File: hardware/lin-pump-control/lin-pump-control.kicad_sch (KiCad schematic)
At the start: 27 parts, among them J1 UPDI, J2 I2C LCD, J3 LINBus, Q1 2N7002, Q2 2N7002, U1 TJA1021T, U2 ATtiny824-X, U3 PCA9536DP

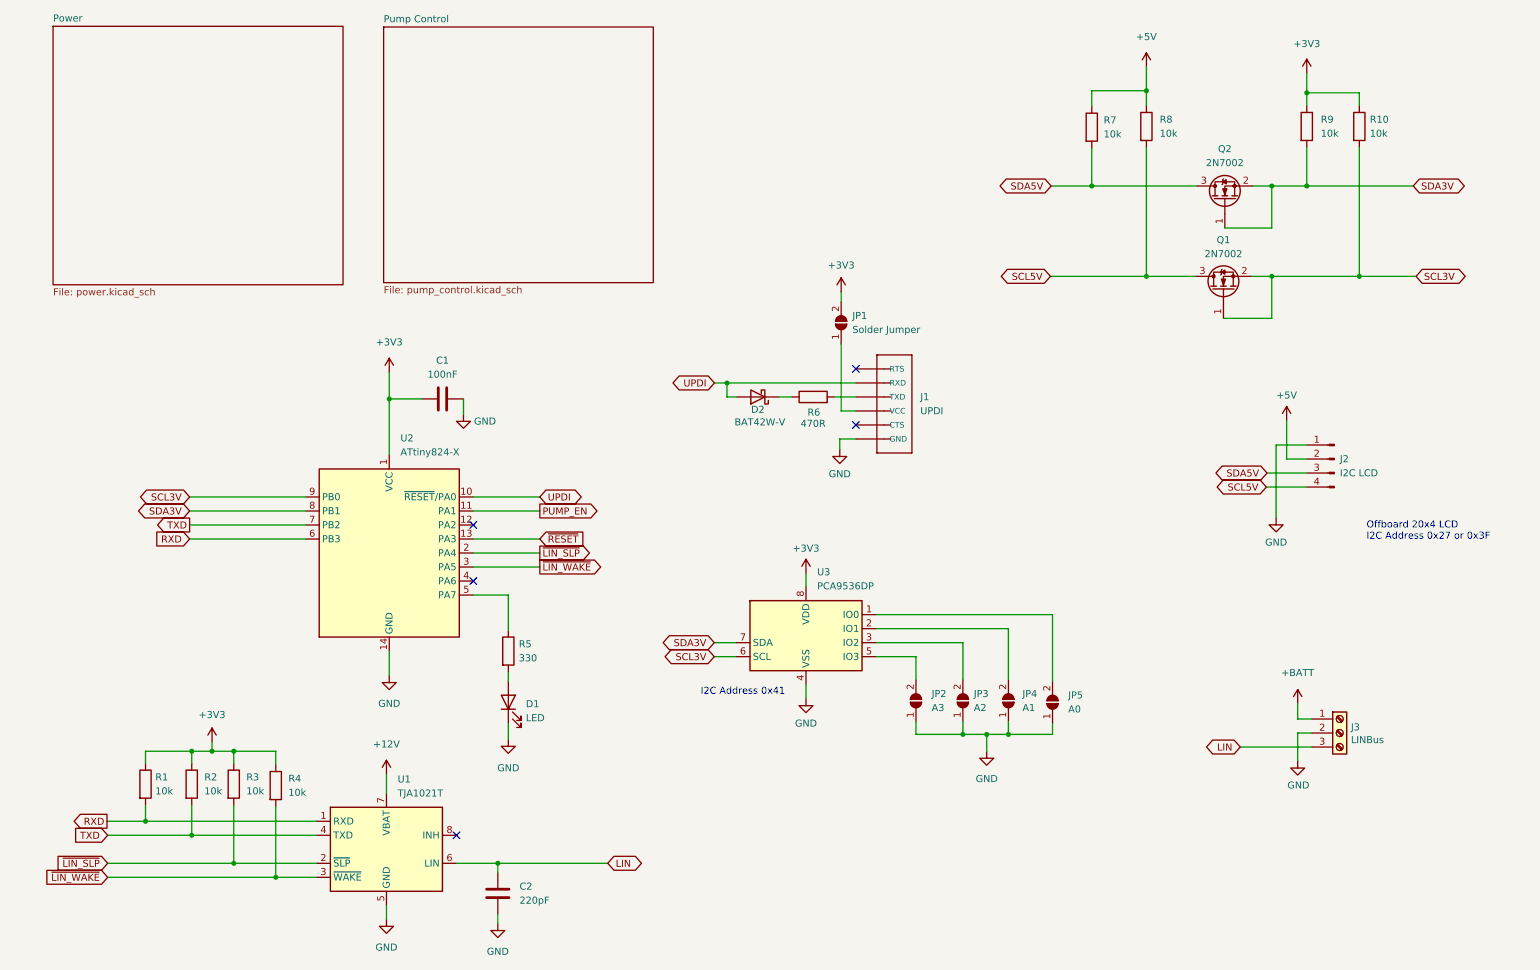
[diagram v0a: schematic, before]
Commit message: Add INA219 to pump controller, change to using regulator module
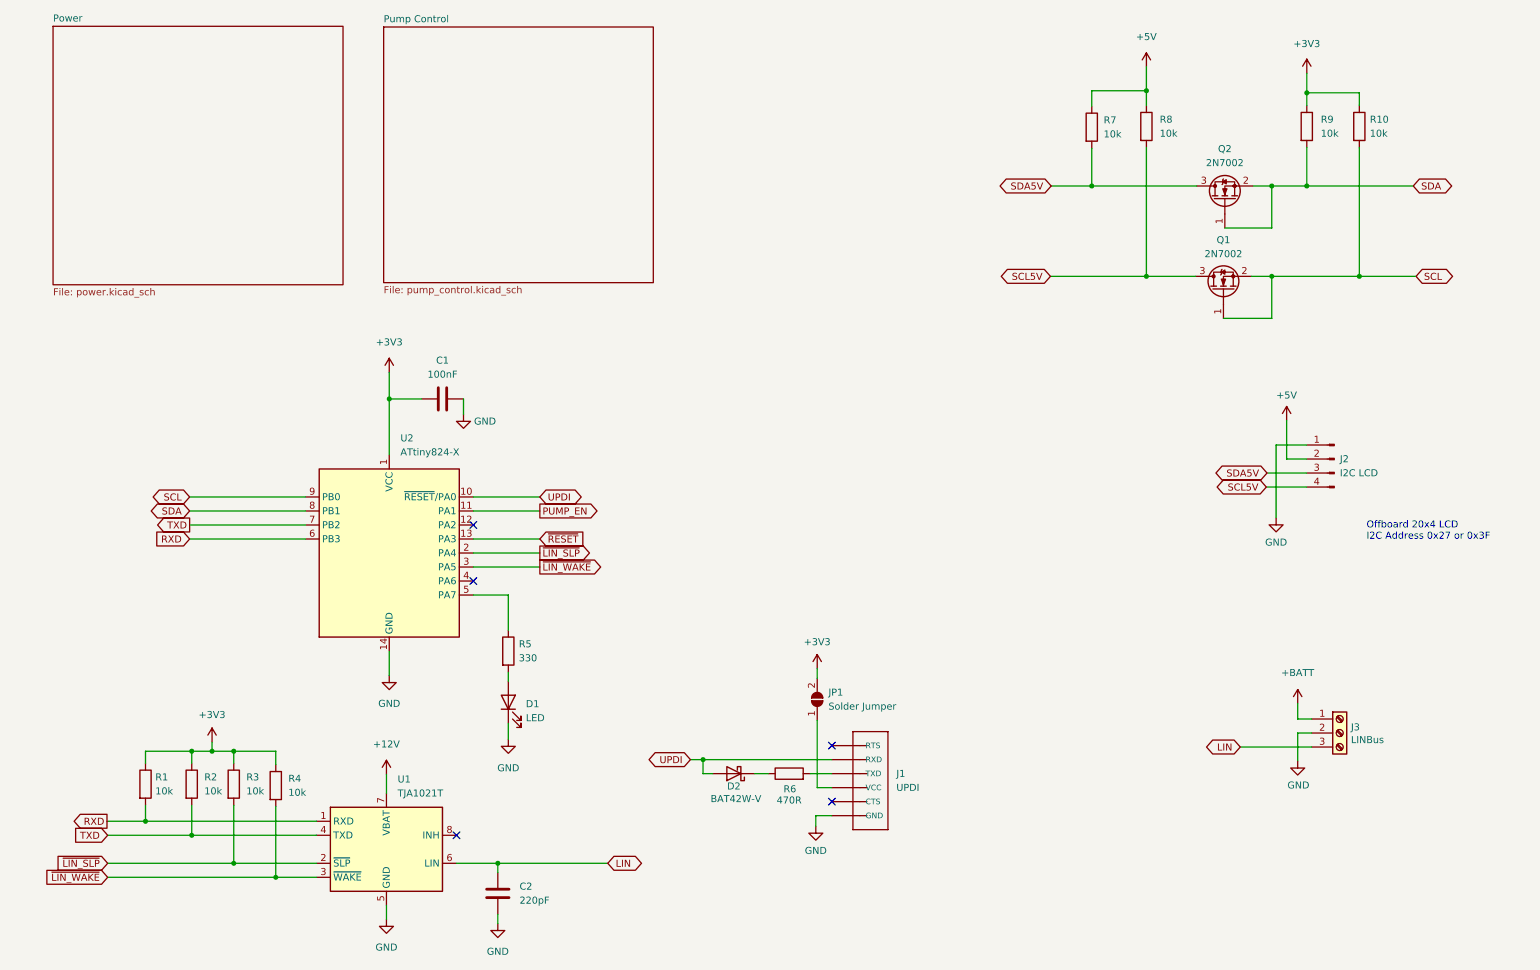
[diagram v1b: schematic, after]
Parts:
- removed JP2: A3, Jumper:SolderJumper-2_P1.3mm_Open_TrianglePad1.0x1.5mm, symbol Jumper:SolderJumper_2_Open
- removed JP3: A2, Jumper:SolderJumper-2_P1.3mm_Open_TrianglePad1.0x1.5mm, symbol Jumper:SolderJumper_2_Open
- removed JP4: A1, Jumper:SolderJumper-2_P1.3mm_Open_TrianglePad1.0x1.5mm, symbol Jumper:SolderJumper_2_Open
- removed JP5: A0, Jumper:SolderJumper-2_P1.3mm_Open_TrianglePad1.0x1.5mm, symbol Jumper:SolderJumper_2_Open
- removed U3: PCA9536DP, Package_SO:TSSOP-8_3x3mm_P0.65mm, symbol Interface_Expansion:PCA9536DP
- J1: footprint Beirdo:FTDI_BASIC -> Beirdo:FTDI-TARGET
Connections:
- net SCL3V renamed SCL
- net SDA3V renamed SDA
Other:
- note removed: "I2C Address 0x41"
- moved on the sheet: D2, J1, JP1, R6

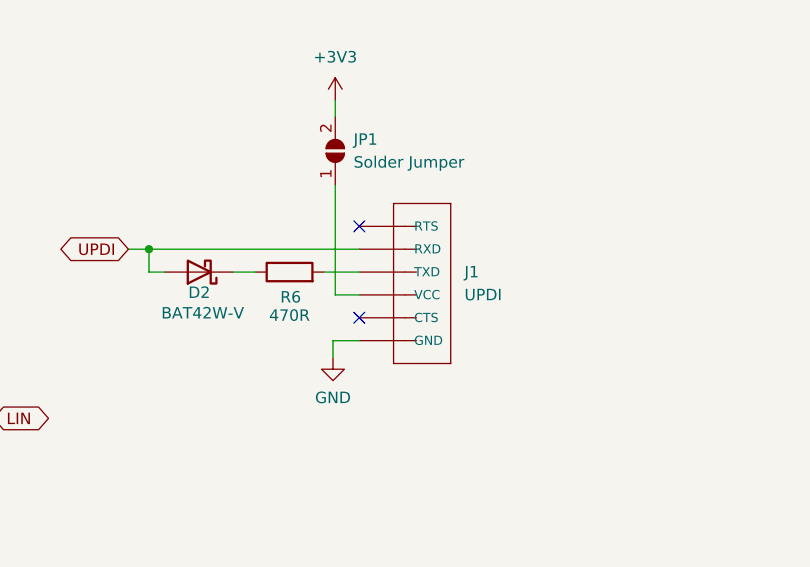
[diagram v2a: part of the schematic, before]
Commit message: Update the schematics... remove PCA9536, use voltage regulator
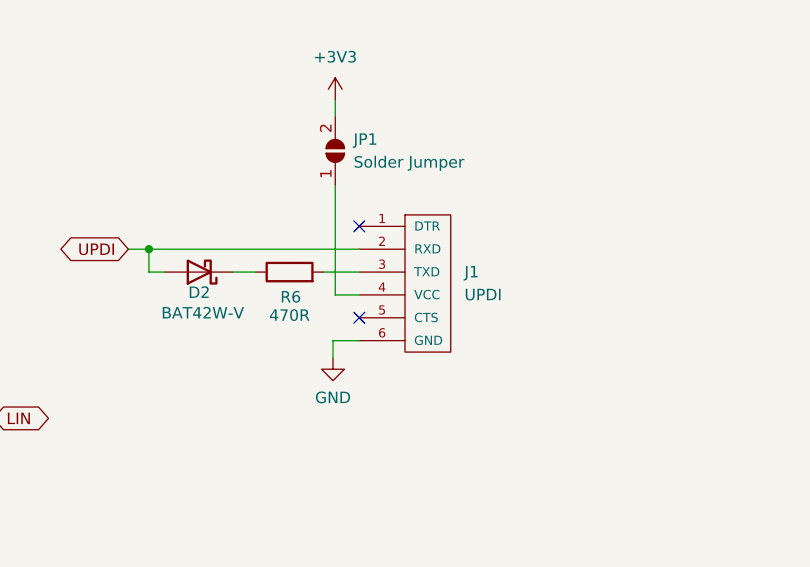
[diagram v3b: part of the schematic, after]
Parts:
- J1: symbol Beirdo:FTDI_BASICPTH -> Beirdo:FTDI-TARGET
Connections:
- net GND: now also J1.6 (GND); no longer J1.1 (GND)
- net UPDI: now also J1.2 (RXD); no longer J1.5 (RXD)
- net at J1.3 (TXD): now also R6.2; no longer JP1.1 (A)
- net at J1.4 (VCC): now also JP1.1 (A); no longer R6.2
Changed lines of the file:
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@@
     (pin "2")
   )
-  (symbol (lib_id "Beirdo:FTDI_BASICPTH") (at 164.846 157.734 0) (mirror y) (unit 1)
+  (symbol (lib_id "Beirdo:FTDI-TARGET") (at 167.386 148.844 0) (unit 1)
     (in_bom yes) (on_board yes) (fields_autoplaced)
     (property "Reference" "J1" (id 0) (at 171.45 155.1939 0)
-      (effects (font (size 1.27 1.27)) (justify right))
+      (effects (font (size 1.27 1.27)) (justify left))
     )
     (property "Value" "UPDI" (id 1) (at 171.45 157.7339 0)
-      (effects (font (size 1.27 1.27)) (justify right))
+      (effects (font (size 1.27 1.27)) (justify left))
     )
-    (property "Footprint" "Beirdo:FTDI-TARGET" (id 2) (at 164.084 153.924 0)
+    (property "Footprint" "Beirdo:FTDI-TARGET" (id 2) (at 167.386 167.894 0)
       (effects (font (size 0.508 0.508)) hide)
     )
